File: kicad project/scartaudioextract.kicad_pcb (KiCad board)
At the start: 2 copper layers, 45.5 x 55.8 mm, 3 parts, among them J1 SCART-F, J2 SCART-F, J3 AudioJack3

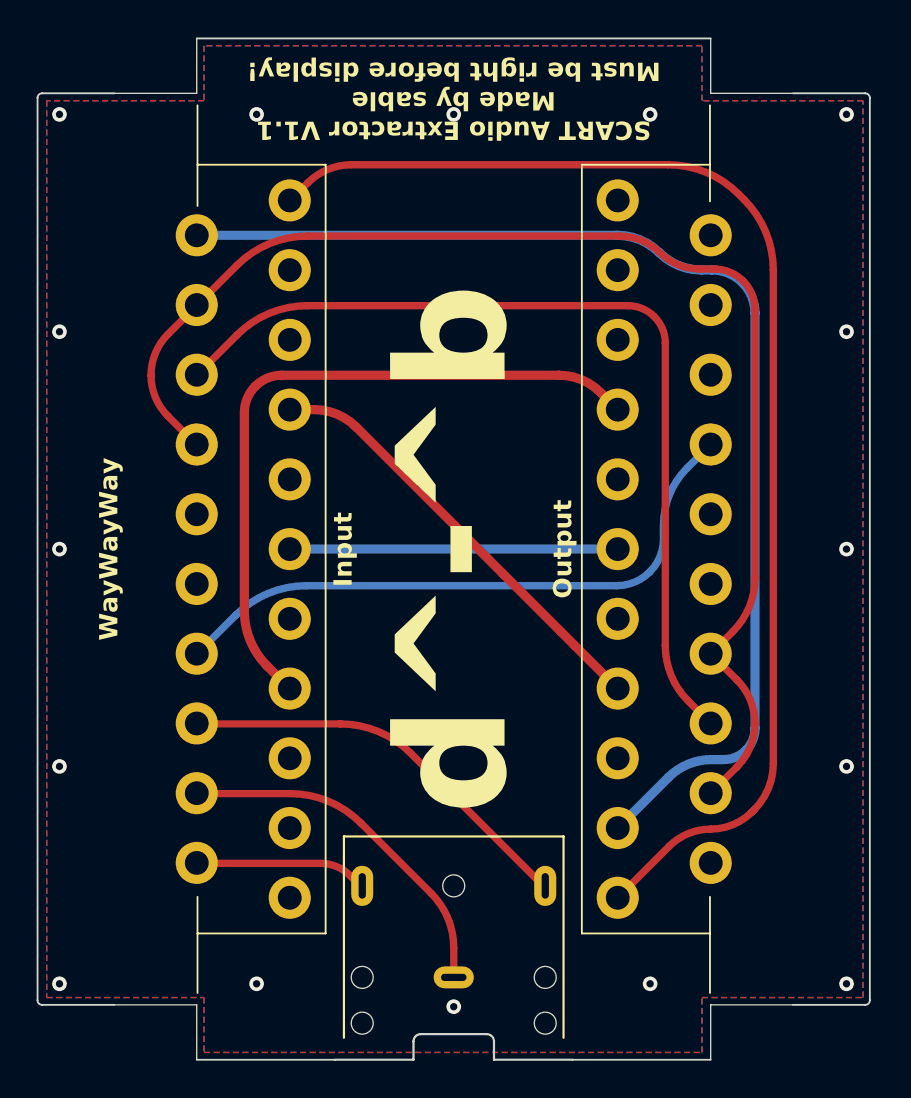
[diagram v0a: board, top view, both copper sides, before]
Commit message: add termination resistors
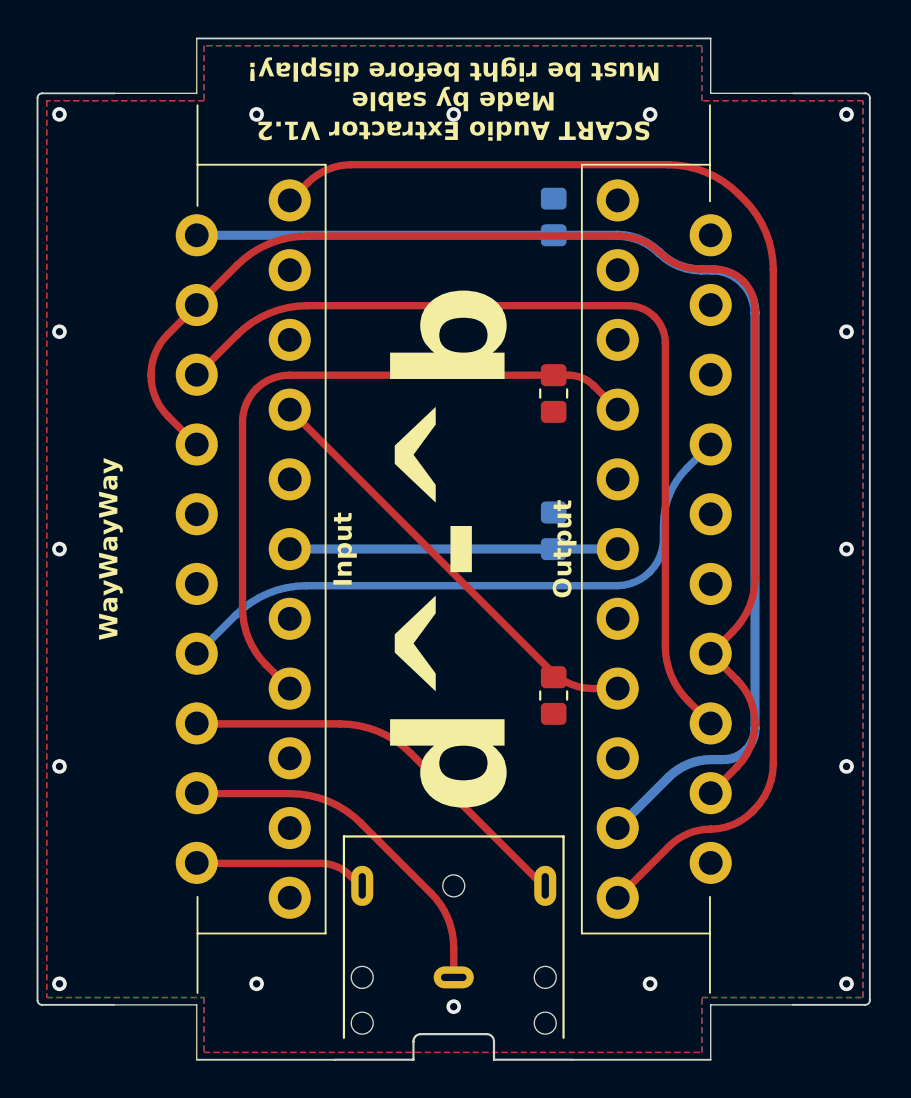
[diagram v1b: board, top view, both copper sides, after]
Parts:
- added R1: 75R0, Resistor_SMD:R_0805_2012Metric_Pad1.20x1.40mm_HandSolder, F.Cu at (154.5, 50.0)
- added R2: 75R0, Resistor_SMD:R_0805_2012Metric_Pad1.20x1.40mm_HandSolder, B.Cu at (154.5, 57.5)
- added R3: 75R0, Resistor_SMD:R_0805_2012Metric_Pad1.20x1.40mm_HandSolder, F.Cu at (154.5, 66.5)
- added R4: 75R0, Resistor_SMD:R_0805_2012Metric_Pad1.20x1.40mm_HandSolder, B.Cu at (154.5, 40.4)
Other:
- board text added: "SCART Audio Extractor V1.2 Made by sable Must be right before display!"
- board text removed: "SCART Audio Extractor V1.1 Made by sable Must be right before display!"

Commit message: remove termination resistors
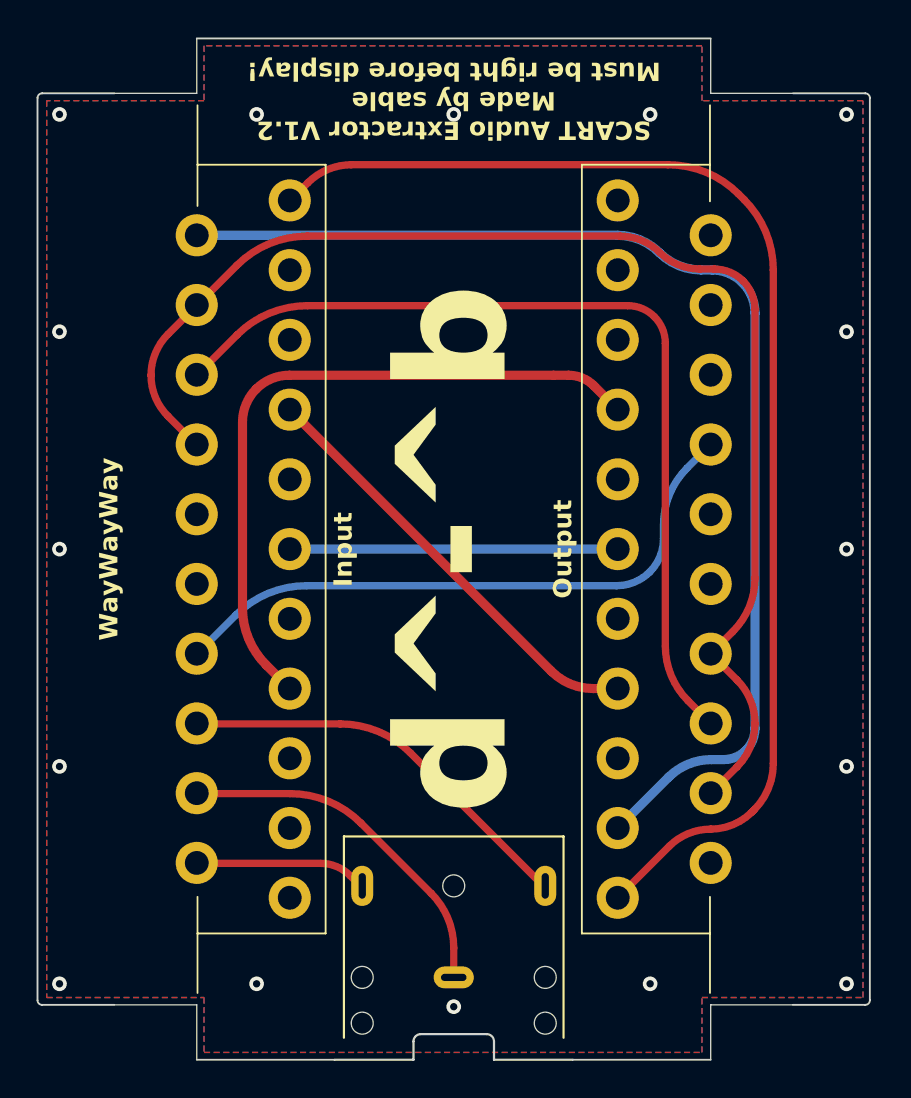
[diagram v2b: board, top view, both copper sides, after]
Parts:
- removed R1, R2, R3, R4: 75R0, Resistor_SMD:R_0805_2012Metric_Pad1.20x1.40mm_HandSolder
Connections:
- J2 pad 5: Video Gnd -> unconnected-(J2-P5-Pad5)

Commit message: forgot a connection
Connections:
- J2 pad 5: unconnected-(J2-P5-Pad5) -> Video Gnd
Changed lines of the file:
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@@
       (usegerberattributes true)
       (usegerberadvancedattributes true)
-      (creategerberjobfile true)
+      (creategerberjobfile false)
       (dashed_line_dash_ratio 12.000000)
       (dashed_line_gap_ratio 3.000000)
@@
       (drillshape 0)
       (scaleselection 1)
-      (outputdirectory "C:/Users/steve/Documents/KiCad/7.0/projects/scartaudioextract/scartaudioextract/scartaudioextract-gerbers")
+      (outputdirectory "C:/Users/leah/Documents/KiCad/7.0/projects/scartaudioextract/scartaudioextract/scartaudioextract-gerbers")
     )
   )
@@
   (net 24 "unconnected-(J2-P20-Pad20)")
   (net 25 "Status{slash}Blanking Gnd")
-  (net 26 "unconnected-(J2-P5-Pad5)")
   (footprint "Connector_Audio:Jack_3.5mm_CUI_SJ1-3523N_Horizontal" (layer "F.Cu")
     (at 149.04 81.9)
@@
       (net 17 "unconnected-(J2-P4-Pad4)") (pinfunction "P4") (pintype "passive+no_connect"))
     (pad "5" thru_hole circle (at -11.43 2.54 270) (size 2.3 2.3) (drill 1.3) (layers "*.Cu" "*.Mask")
-      (net 26 "unconnected-(J2-P5-Pad5)") (pinfunction "P5") (pintype "passive"))
+      (net 2 "Video Gnd") (pinfunction "P5") (pintype "passive"))
     (pad "6" thru_hole circle (at -9.525 -2.54 270) (size 2.3 2.3) (drill 1.3) (layers "*.Cu" "*.Mask")
       (net 18 "unconnected-(J2-P6-Pad6)") (pinfunction "P6") (pintype "passive+no_connect"))

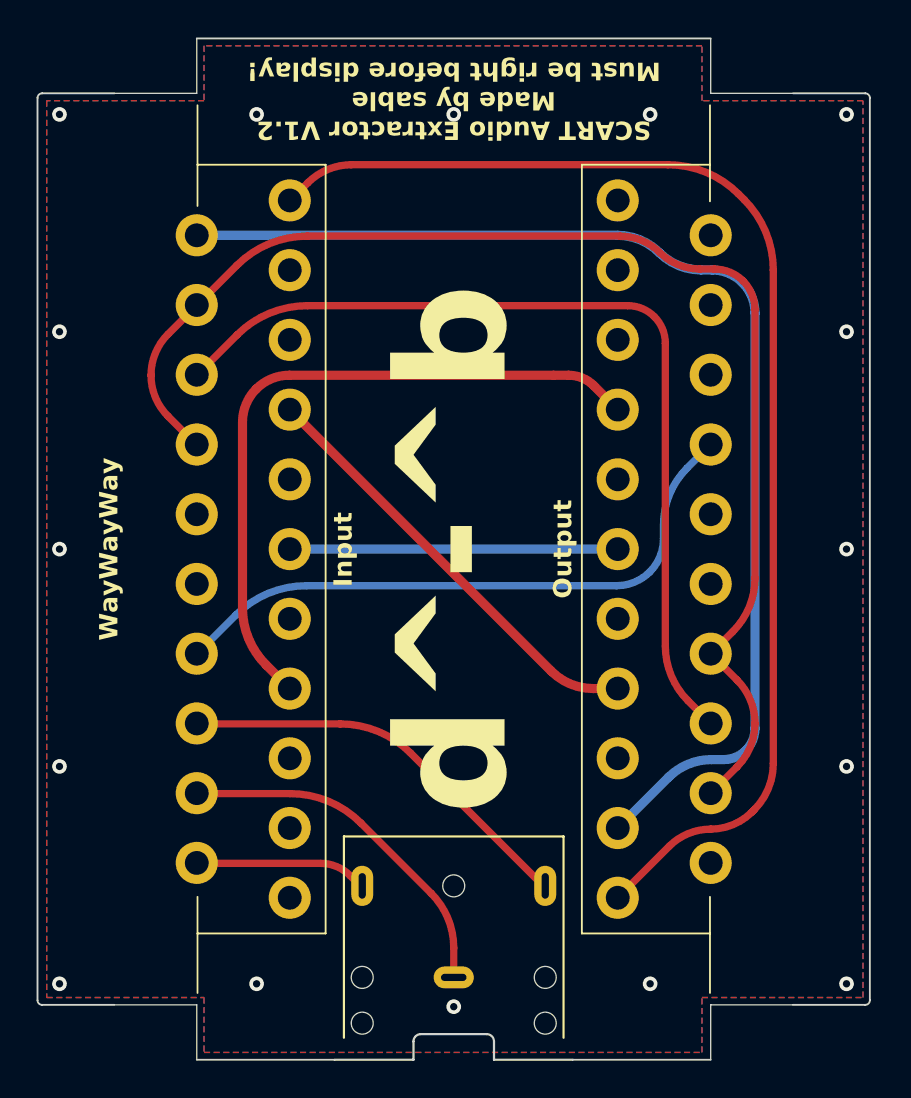
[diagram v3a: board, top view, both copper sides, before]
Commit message: improve schematic, use better design rules
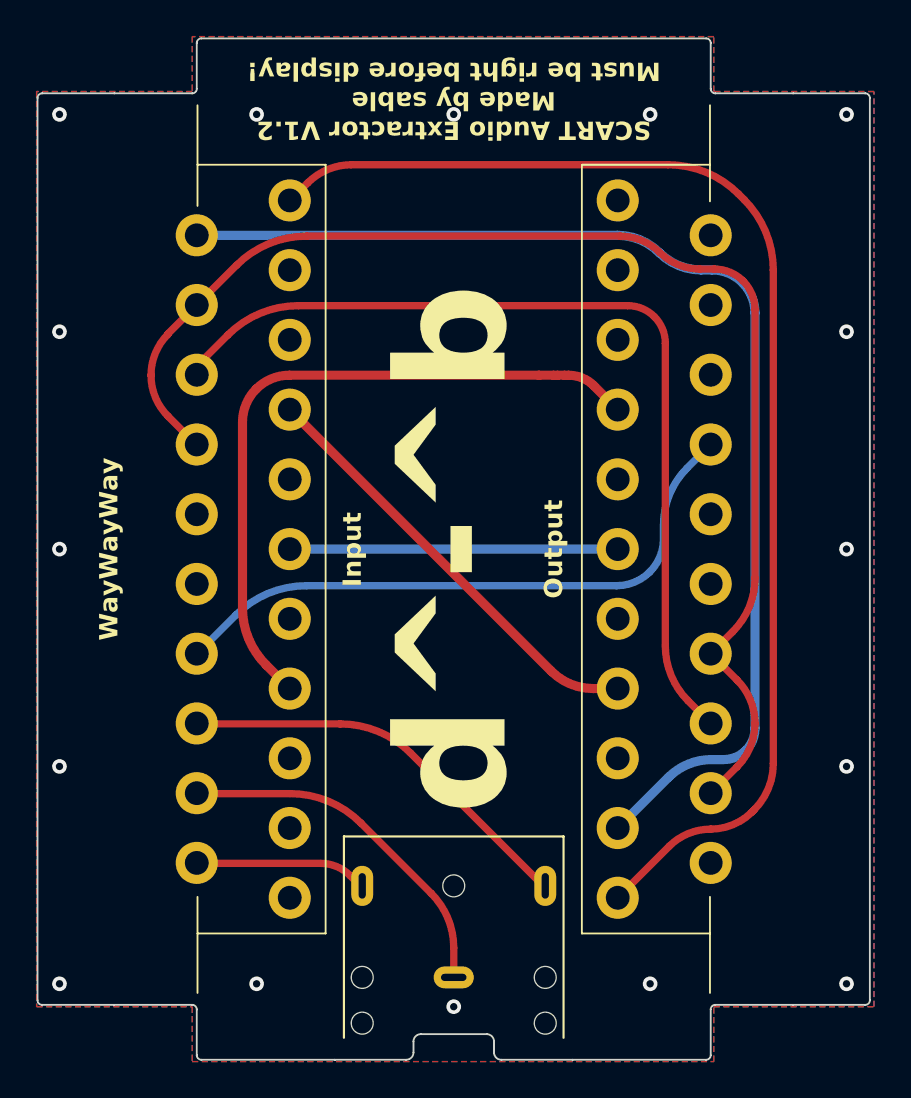
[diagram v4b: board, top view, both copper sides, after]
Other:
- outline, holes or cut-outs redrawn
